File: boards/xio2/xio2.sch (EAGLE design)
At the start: 362 parts, among them J1 12401598E4#2A, Q1 BSS138, Q2 BSS138, Q3 BC817-16LT3G, Q4 BC817-16LT3G, Y2 FA-238 25.0000MB-K3

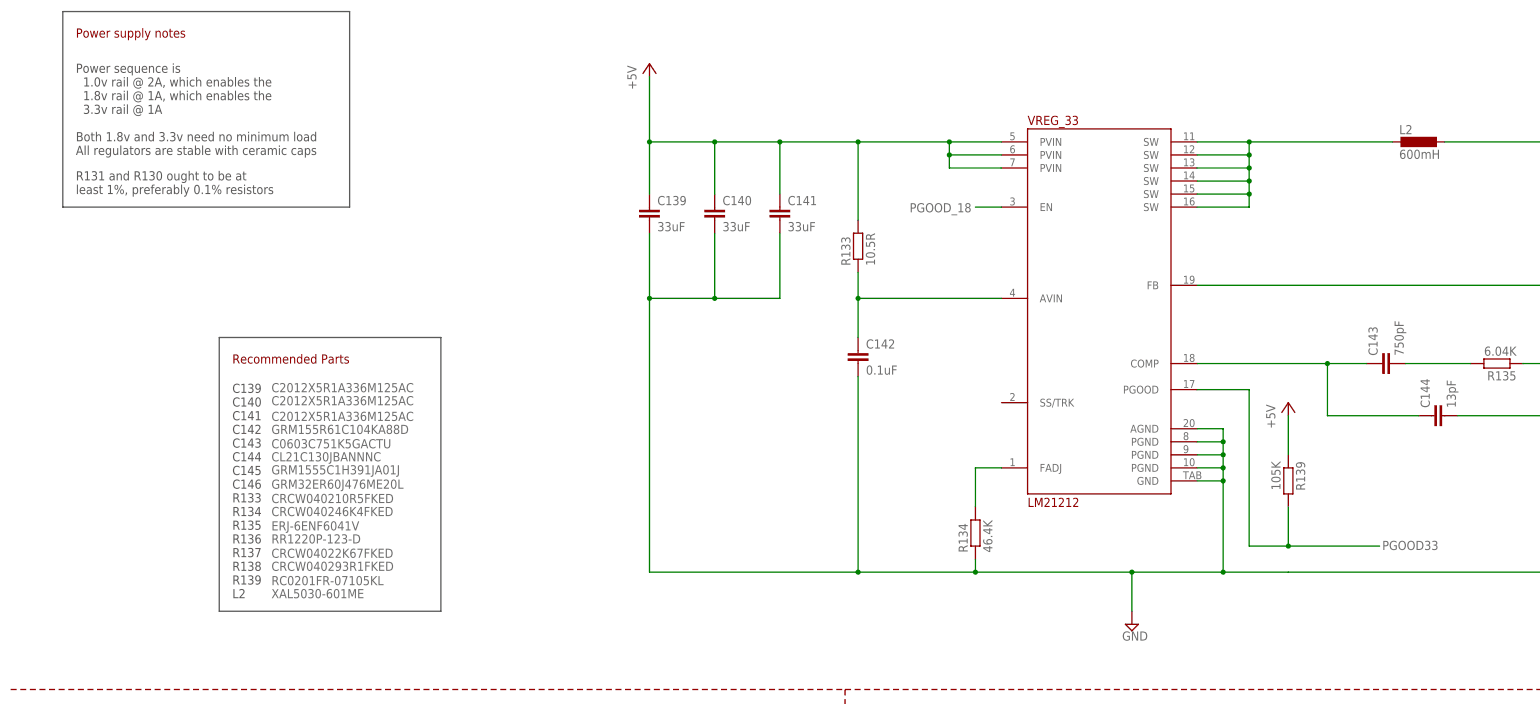
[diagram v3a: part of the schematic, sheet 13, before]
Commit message: Changes for the new inductor in the power-supply section
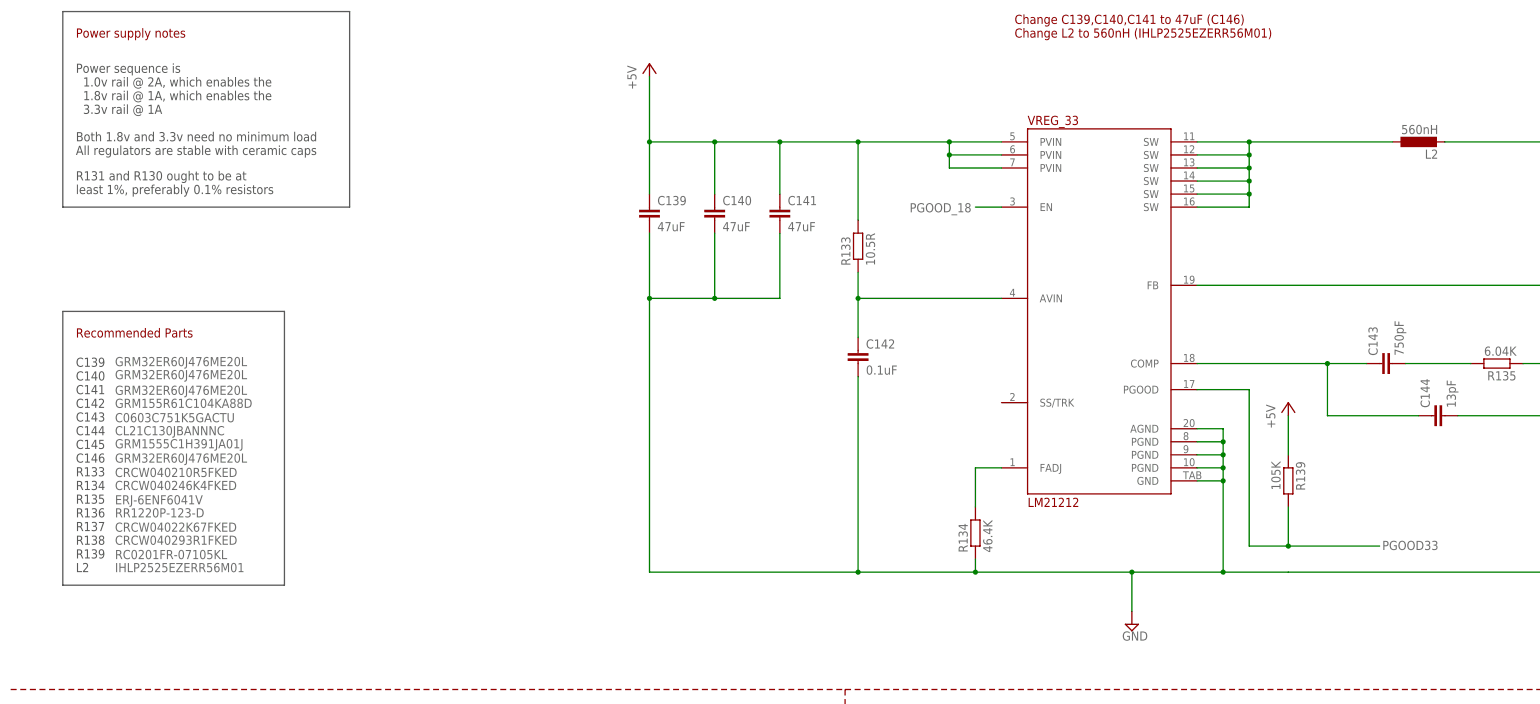
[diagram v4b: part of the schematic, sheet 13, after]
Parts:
- C13, C167, C168, C169, C170, C171, C172, C19, C20, C21, C22, C23, C24: USE GRM155C80J106ME11D -> GRM033R61A104ME15D
- C139, C140, C141: value 33uF -> 47uF; device rcl:C-EUC2012 -> rcl:C-EUC1210; USE C2012X5R1A336M125AC -> GRM32ER60J476ME20L
- C173: USE GRM033R61A104ME15D -> CL03A105MP3ZSNH
- C58: USE GRM155R60J475ME87D -> GRM033R60J474KE90D
- C97: USE GRM033R60J105MEA2D -> CL03A105MP3ZSNH
- L2: value 600mH -> 560nH; device sjg-power:XAL5030-601MEB -> sjg-inductor:IHLP2525EZERR56M01; USE XAL5030-601ME -> IHLP2525EZERR56M01
- R125, R126, R127: USE RMCF0402JT47K0 -> RMCF0201JT47K0
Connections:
- net +3V3: now also L2.2; no longer L2.1
- net SW_OUT: now also L2.1; no longer L2.2
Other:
- note added: "Change C139,C140,C141 to 47uF (C146) Change L2 to 560nH (IHLP2525EZERR56M01)"
- moved on the sheet: L2

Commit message: Updated board and schematic - all parts now from Seeed library
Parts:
- C10, C100, C106, C113, C114, C115, C116, C117, C118, C119, C120, C121, C122, C123, C124, C125, C126, C127, C128, C129, C13, C130, C131, C132, C133, C134, C137, C138, C16, C167, C168, C169, C170, C171, C172, C19, C2, C20, C21, C22, C23, C24, C25, C26, C27, C28, C29, C3, C31, C32, C33, C35, C4, C5, C53, C54, C55, C56, C57, C6, C60, C61, C62, C63, C64, C65, C66, C67, C68, C69, C7, C70, C71, C72, C8, C80, C81, C87, C88, C89, C9, C90, C91, C92, C94, C96, C98: USE GRM033R61A104ME15D -> GRM033C71C104KE14D

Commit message: Updates to the latest revision for the reddit review
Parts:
- added C37, C38, C39, C40: 0.1uF, rcl:C-EUC0201
- added IC1: MCP604SL, linear:MCP604SL
- SERIAL_BUF0: value MAX3232CDR -> MAX3232ECDR
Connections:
- new net VGA_BLUE: D3.C1A2, IC1C.+IN, R42.1, R43.1, R44.1, R45.1, R46.1, R47.1, R48.1, R49.1
- new net VGA_GRN: D4.C1A2, IC1B.+IN, R28.1, R29.1, R30.1, R31.1, R32.1, R33.1, R34.1, R35.1
- new net VGA_RED: D5.C1A2, IC1A.+IN, R10.1, R13.1, R19.1, R20.1, R22.1, R23.1, R24.1, R25.1
- net +3V3: now also C37.1, C38.1, C39.1, C40.1, IC1P.V+
- net GND: now also C37.2, C38.2, C39.2, C40.2, IC1P.V-
- net VGA_B: now also IC1C.-IN, IC1C.OUT; no longer D3.C1A2, R42.1, R43.1, R44.1, R45.1, R46.1, R47.1, R48.1, R49.1
- net VGA_G: now also IC1B.-IN, IC1B.OUT; no longer D4.C1A2, R28.1, R29.1, R30.1, R31.1, R32.1, R33.1, R34.1, R35.1
- net VGA_R: now also IC1A.-IN, IC1A.OUT; no longer D5.C1A2, R10.1, R13.1, R19.1, R20.1, R22.1, R23.1, R24.1, R25.1
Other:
- note added: "Pull-ups for the JTAG lines"
- note added: "Replace 0.1uF cap on SD socket with 1u, 10u and 22u in parallel"
- note added: "VCCAUX @ 1.8v"
- note added: "VCCIO @ 3.3v"
- note removed: "Need decoupling caps on line drivers"
- moved on the sheet: D1, D2, D3, D4, D5, Q1, Q2, R10, R13, R19, R20, R22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

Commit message: Update to a supported flash type
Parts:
- FPGA_CFG: USE MX25L3206EM2I-12G -> MT25QU128ABA1ESE-0SIT TR
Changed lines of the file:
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@@
 <part name="FRAME12" library="frames" library_urn="urn:adsk.eagle:library:229" deviceset="A3L-LOC" device=""/>
 <part name="FPGA_CFG" library="microbuilder" deviceset="SPIFLASH_SOIC8" device="" value="W25Q80DVSNIG">
-<attribute name="USE" value="MX25L3206EM2I-12G"/>
+<attribute name="USE" value="MT25QU128ABA1ESE-0SIT TR"/>
 </part>
 <part name="SUPPLY37" library="supply2" deviceset="GND" device=""/>
